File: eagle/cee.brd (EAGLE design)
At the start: 50 x 80 mm, 53 parts, among them IC1 IC1, J1 SOLDERJUMPERNC2

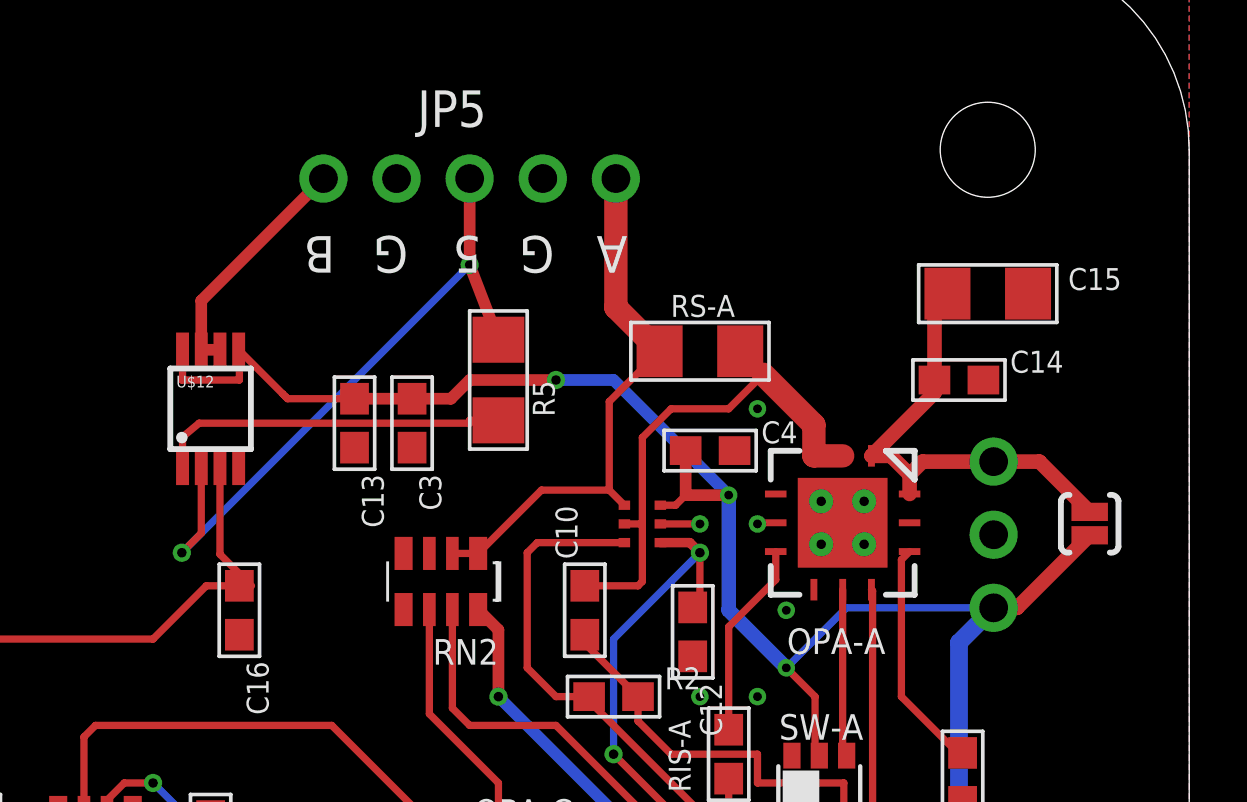
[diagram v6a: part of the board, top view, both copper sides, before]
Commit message: pulldown resistor, chanB as input, moved capacitors, updated sc70, cleaned routing
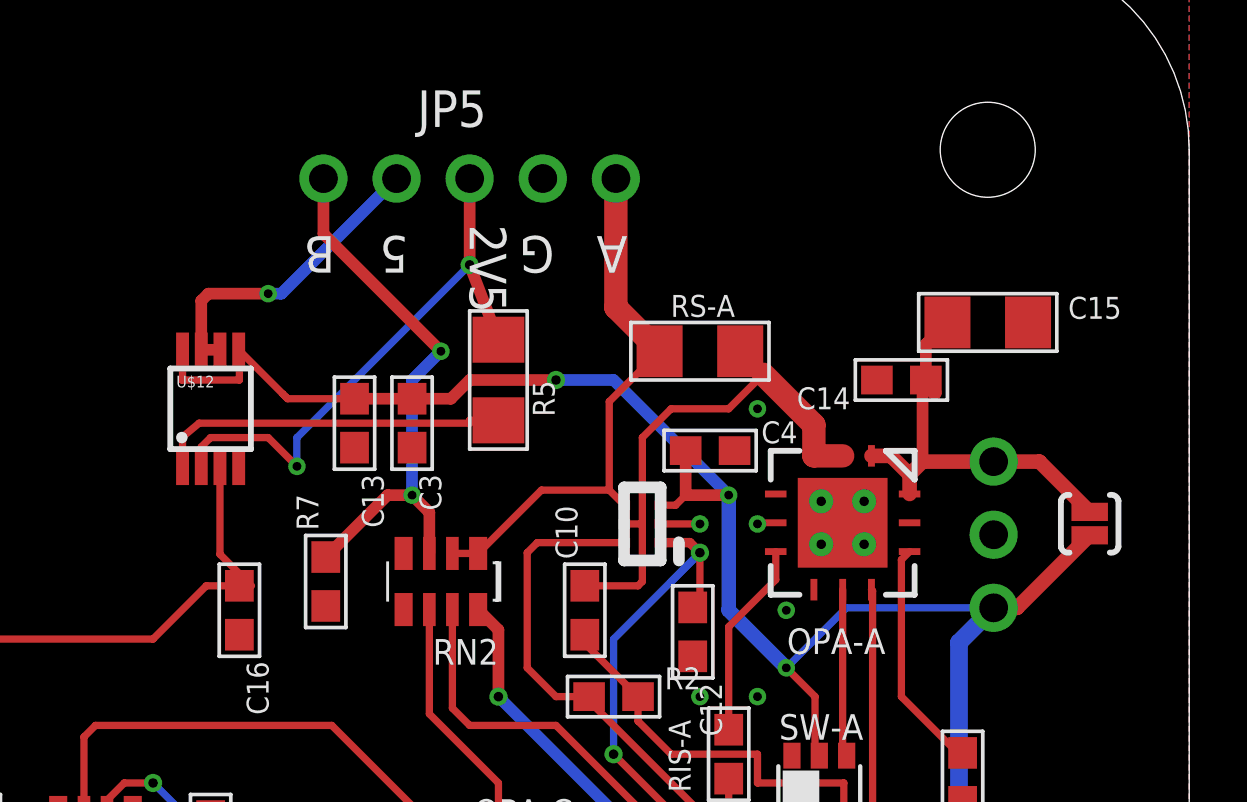
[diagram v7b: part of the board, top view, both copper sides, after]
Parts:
- added R7: (no value), nonolith:0603
- moved C14 2.00 mm to (40.0, 65.0), turned to 180 degrees
- moved C15 1.00 mm to (43.0, 67.0)
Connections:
- new net IN-B: JP5.5, R7.2, RN2.3
- net 5VOUT: now also JP5.4; no longer JP5.5
- net GND: now also R7.1; no longer JP5.4
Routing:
- net IN-B: track 0.00 -> 19.3 mm, vias 0 -> 2
- net 2.5VOUT: track 23.2 -> 19.9 mm
- net 5VOUT: track 8.36 -> 10.9 mm, vias 0 -> 1
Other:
- board text added: "2V5"
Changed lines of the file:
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@@
 <text x="7.366" y="11.176" size="0.762" layer="25" font="vector" ratio="11" rot="R180">5v</text>
 <text x="14.335" y="2.54" size="1.016" layer="25" font="vector" ratio="12" align="center">2.0 beta 1</text>
-<text x="22.86" y="70" size="1.27" layer="25" font="vector" ratio="12" rot="SR180">G</text>
-<text x="25.4" y="70" size="1.27" layer="25" font="vector" ratio="12" rot="SR180">5</text>
+<text x="22.86" y="70" size="1.27" layer="25" font="vector" ratio="12" rot="SR180">5</text>
+<text x="25" y="70.4" size="1.27" layer="25" font="vector" ratio="12" rot="SR270">2V5</text>
 <text x="27.94" y="70" size="1.27" layer="25" font="vector" ratio="12" rot="SR180">G</text>
 <text x="9.906" y="11.176" size="0.762" layer="25" font="vector" ratio="11" rot="R180">GND</text>
@@
 <attribute name="VALUE" x="35.2938" y="47.5682" size="0.889" layer="27" font="vector" ratio="12"/>
 </element>
-<element name="C14" library="nonolith" package="0603" value=".1uF" x="42" y="65"/>
-<element name="C15" library="nonolith" package="1206" value="47uF" x="43" y="68"/>
+<element name="C14" library="nonolith" package="0603" value=".1uF" x="40" y="65" rot="R180"/>
+<element name="C15" library="nonolith" package="1206" value="47uF" x="43" y="67"/>
 <element name="J1" library="SparkFun" package="SJ_2S-NOTRACE" value="SOLDERJUMPERNC2" x="46.542" y="60.006" smashed="yes" rot="R90"/>
 <element name="C4" library="nonolith" package="0603" value=".1uF" x="33.355" y="62.548" smashed="yes" rot="R180">
@@
 <element name="C13" library="nonolith" package="0603" value=".1uF" x="21" y="63.5" rot="R270"/>
 <element name="C16" library="nonolith" package="0603" value="" x="17" y="57" rot="R270"/>
+<element name="R7" library="nonolith" package="0603" value="" x="20" y="58" rot="R90"/>
 </elements>
 <signals>
@@
 <contactref element="JP1" pad="2"/>
 <contactref element="JP5" pad="2"/>
-<contactref element="JP5" pad="4"/>
 <contactref element="EXPANSION" pad="5"/>
 <polygon width="0.4064" layer="16" isolate="0.3048" rank="3">
@@
 <contactref element="C16" pad="2"/>
 <via x="30.5" y="30.25" extent="1-16" drill="0.3302" shape="octagon"/>
+<contactref element="R7" pad="1"/>
 </signal>
 <signal name="PDI-DATA">
@@
 <contactref element="J1" pad="2"/>
 <contactref element="JP1" pad="3"/>
-<wire x1="41.15" y1="65" x2="41.15" y2="67.55" width="0.508" layer="1"/>
-<wire x1="41.15" y1="67.55" x2="41.6" y2="68" width="0.508" layer="1"/>
+<wire x1="41.15" y1="67.55" x2="41.6" y2="67" width="0.508" layer="1"/>
 <wire x1="38.96" y1="62.365" x2="39.635" y2="62.365" width="0.508" layer="1"/>
 <wire x1="39.635" y1="62.365" x2="40.285" y2="61.715" width="0.508" layer="1"/>
 <wire x1="40.285" y1="61.715" x2="40.285" y2="61.04" width="0.508" layer="1"/>
-<wire x1="38.96" y1="62.365" x2="41.15" y2="64.555" width="0.508" layer="1"/>
-<wire x1="41.15" y1="64.555" x2="41.15" y2="65" width="0.508" layer="1"/>
+<wire x1="41.15" y1="64.555" x2="40.85" y2="65" width="0.508" layer="1"/>
 <wire x1="40.285" y1="61.715" x2="40.735" y2="62.165" width="0.508" layer="1"/>
 <wire x1="40.735" y1="62.165" x2="43.2052" y2="62.165" width="0.508" layer="1"/>
 <wire x1="43.2052" y1="62.165" x2="44.7957" y2="62.165" width="0.508" layer="1"/>
 <wire x1="44.7957" y1="62.165" x2="46.542" y2="60.4187" width="0.508" layer="1"/>
+<wire x1="40.735" y1="62.165" x2="40.735" y2="64.885" width="0.4064" layer="1"/>
+<wire x1="40.735" y1="64.885" x2="40.85" y2="65" width="0.4064" layer="1"/>
+<wire x1="40.85" y1="65" x2="40.85" y2="66.25" width="0.4064" layer="1"/>
+<wire x1="40.85" y1="66.25" x2="41.6" y2="67" width="0.4064" layer="1"/>
 </signal>
 <signal name="BOOTLOAD">
@@
 </signal>
 <signal name="5VOUT">
-<contactref element="JP5" pad="5"/>
 <contactref element="U$12" pad="7"/>
 <contactref element="U$12" pad="6"/>
 <wire x1="16.325" y1="66.05" x2="15.675" y2="66.05" width="0.4064" layer="1"/>
-<wire x1="15.675" y1="67.755" x2="19.92" y2="72" width="0.4064" layer="1"/>
 <wire x1="15.675" y1="67.755" x2="15.675" y2="66.05" width="0.4064" layer="1"/>
+<contactref element="JP5" pad="4"/>
+<wire x1="15.675" y1="67.755" x2="15.92" y2="68" width="0.4064" layer="1"/>
+<wire x1="15.92" y1="68" x2="18" y2="68" width="0.4064" layer="1"/>
+<via x="18" y="68" extent="1-16" drill="0.305"/>
+<wire x1="18" y1="68" x2="18.46" y2="68" width="0.4064" layer="16"/>
+<wire x1="18.46" y1="68" x2="22.46" y2="72" width="0.4064" layer="16"/>
 </signal>
 <signal name="2.5VOUT">
@@
 <wire x1="25" y1="69" x2="26" y2="66.4" width="0.4064" layer="1"/>
 <wire x1="25" y1="72" x2="25" y2="69" width="0.4064" layer="1"/>
-<wire x1="15.675" y1="59.675" x2="15" y2="59" width="0.254" layer="1"/>
-<via x="15" y="59" extent="1-16" drill="0.3302"/>
-<wire x1="15" y1="59" x2="25" y2="69" width="0.254" layer="16"/>
-<wire x1="15.675" y1="59.675" x2="15.675" y2="61.95" width="0.254" layer="1"/>
+<wire x1="15.675" y1="61.95" x2="15.675" y2="62.675" width="0.254" layer="1"/>
+<wire x1="15.675" y1="62.675" x2="16" y2="63" width="0.254" layer="1"/>
+<wire x1="16" y1="63" x2="18" y2="63" width="0.254" layer="1"/>
+<wire x1="18" y1="63" x2="19" y2="62" width="0.254" layer="1"/>
+<via x="19" y="62" extent="1-16" drill="0.305"/>
+<wire x1="19" y1="62" x2="19" y2="63" width="0.254" layer="16"/>
+<wire x1="19" y1="63" x2="25" y2="69" width="0.254" layer="16"/>
 </signal>
 <signal name="2.5VFDBK">
@@
 <wire x1="25" y1="63.6" x2="26" y2="63.6" width="0.254" layer="1"/>
 </signal>
+<signal name="IN-B">
+<contactref element="RN2" pad="3"/>
+<contactref element="JP5" pad="5"/>
+<wire x1="23.6" y1="58.975" x2="23.6" y2="60.4" width="0.4064" layer="1"/>
+<wire x1="23.6" y1="60.4" x2="23" y2="61" width="0.4064" layer="1"/>
+<via x="23" y="61" extent="1-16" drill="0.305"/>
+<wire x1="23" y1="61" x2="23" y2="65" width="0.4064" layer="16"/>
+<wire x1="23" y1="65" x2="24" y2="66" width="0.4064" layer="16"/>
+<via x="24" y="66" extent="1-16" drill="0.305"/>
+<wire x1="24" y1="66" x2="19.92" y2="70.08" width="0.4064" layer="1"/>
+<wire x1="19.92" y1="70.08" x2="19.92" y2="72" width="0.4064" layer="1"/>
+<contactref element="R7" pad="2"/>
+<wire x1="20" y1="58.85" x2="22.15" y2="61" width="0.4064" layer="1"/>
+<wire x1="22.15" y1="61" x2="23" y2="61" width="0.4064" layer="1"/>
+</signal>
 </signals>
-<errors>
-</errors>
 </board>
 </drawing>

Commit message: route tflag
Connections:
- new net TFLAG-P: IC1.5, R4.2
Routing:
- net TFLAG-P: track 0.00 -> 31.6 mm, vias 0 -> 2
- net ISET-DAC-A: track 27.3 -> 29.1 mm
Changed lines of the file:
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@@
 <wire x1="23" y1="3" x2="31" y2="3" width="0.508" layer="16"/>
 <wire x1="31" y1="3" x2="42" y2="14" width="0.508" layer="16"/>
-<wire x1="42" y1="14" x2="42" y2="32" width="0.508" layer="16"/>
+<wire x1="42" y1="14" x2="42" y2="32" width="0.4096" layer="16"/>
 <wire x1="41.5" y1="14" x2="42" y2="14" width="0.508" layer="16"/>
 <via x="21" y="7" extent="1-16" drill="0.381" shape="octagon"/>
@@
 <wire x1="28" y1="65" x2="30" y2="65" width="0.4064" layer="16"/>
 <wire x1="30" y1="65" x2="34" y2="61" width="0.4064" layer="16"/>
-<wire x1="42" y1="32" x2="42" y2="55.8798" width="0.6096" layer="16"/>
+<wire x1="42" y1="32" x2="42" y2="55.8798" width="0.4064" layer="16"/>
 <wire x1="42" y1="55.8798" x2="43.2052" y2="57.085" width="0.6096" layer="16"/>
 <wire x1="21" y1="64.35" x2="23" y2="64.35" width="0.4064" layer="1"/>
@@
 <contactref element="RIS-A" pad="1"/>
 <contactref element="IC1" pad="6"/>
-<wire x1="25" y1="30.75" x2="25" y2="33" width="0.254" layer="1"/>
-<via x="25" y="33" extent="1-16" drill="0.305"/>
-<wire x1="25" y1="33" x2="29" y2="33" width="0.254" layer="16"/>
-<wire x1="29" y1="33" x2="35" y2="39" width="0.254" layer="16"/>
+<wire x1="25" y1="30.75" x2="25" y2="36" width="0.254" layer="1"/>
+<via x="25" y="36" extent="1-16" drill="0.305"/>
 <via x="34" y="48" extent="1-16" drill="0.305"/>
 <wire x1="34" y1="48" x2="34" y2="51.15" width="0.254" layer="1"/>
@@
 <wire x1="35" y1="39" x2="35" y2="47" width="0.254" layer="1"/>
 <wire x1="35" y1="47" x2="34" y2="48" width="0.254" layer="1"/>
+<wire x1="25" y1="36" x2="32" y2="36" width="0.254" layer="16"/>
+<wire x1="32" y1="36" x2="35" y2="39" width="0.254" layer="16"/>
 </signal>
 <signal name="SMUP-B">
@@
 <wire x1="22.15" y1="61" x2="23" y2="61" width="0.4064" layer="1"/>
 </signal>
+<signal name="TFLAG-P">
+<contactref element="R4" pad="2"/>
+<contactref element="IC1" pad="5"/>
+<wire x1="42.1264" y1="50.3444" x2="42.1264" y2="42.1264" width="0.254" layer="1"/>
+<wire x1="42.1264" y1="42.1264" x2="35" y2="35" width="0.254" layer="1"/>
+<via x="35" y="35" extent="1-16" drill="0.305"/>
+<wire x1="35" y1="35" x2="26" y2="35" width="0.254" layer="16"/>
+<via x="26" y="35" extent="1-16" drill="0.305"/>
+<wire x1="26" y1="35" x2="25.8" y2="34.8" width="0.254" layer="1"/>
+<wire x1="25.8" y1="34.8" x2="25.8" y2="30.75" width="0.254" layer="1"/>
+</signal>
 </signals>
